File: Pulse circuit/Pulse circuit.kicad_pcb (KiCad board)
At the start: 4 copper layers, 76.9 x 88 mm, 9 parts, among them J1 Conn_01x02_Pin, U1 module_max30102, U2 module_max30102, U3 DOIT-ESP32-DEVKIT-V1

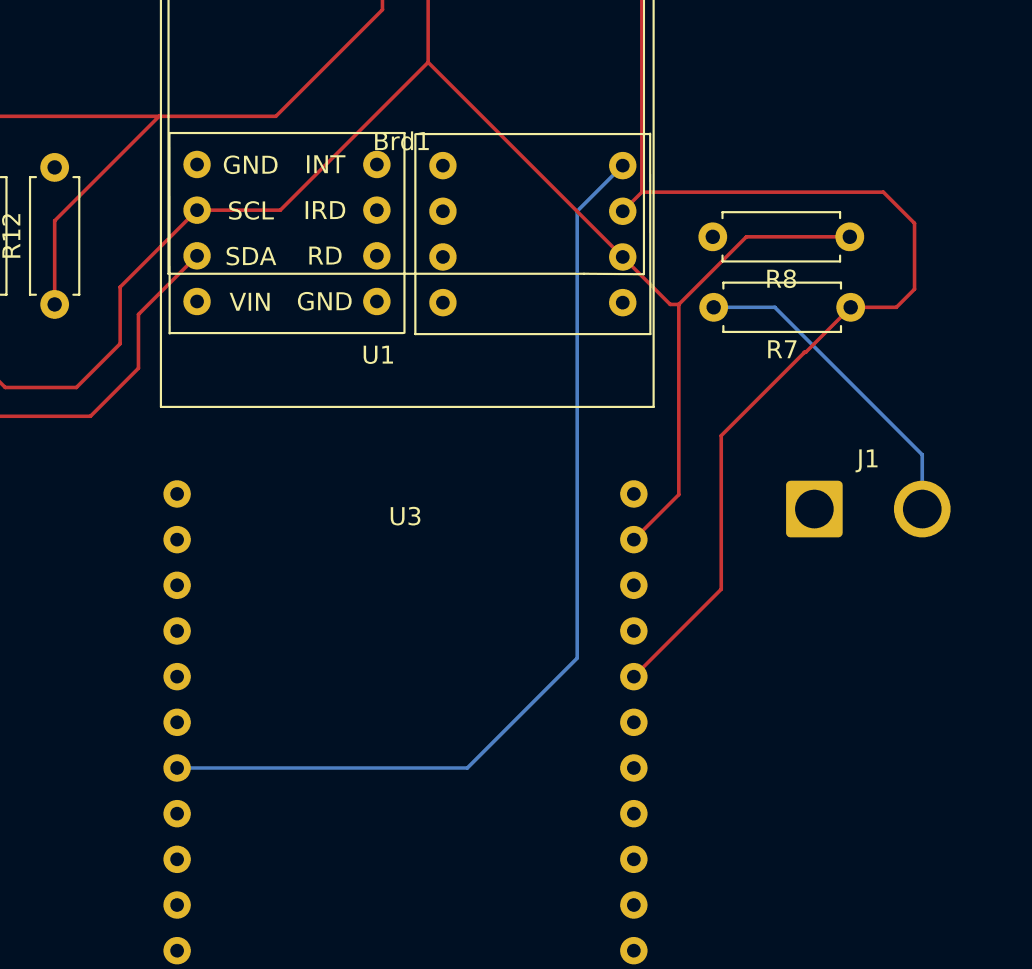
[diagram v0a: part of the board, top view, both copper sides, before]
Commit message: PCB new layer routed
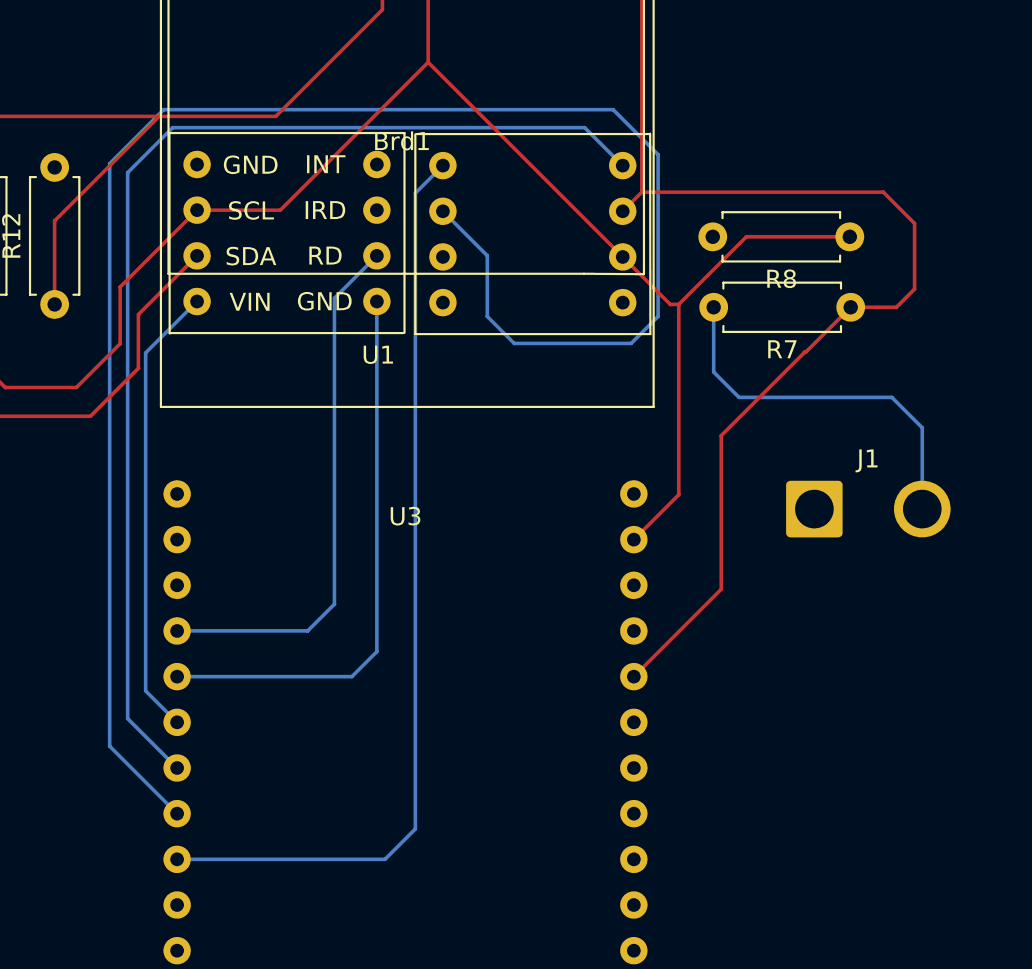
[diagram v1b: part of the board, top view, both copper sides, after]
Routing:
- net RD5v: track 0.00 -> 97.1 mm
- net IRD5v: track 0.02 -> 51.5 mm
- net IRD3v3: track 0.00 -> 31.2 mm
- net RD3v3: track 0.00 -> 29.7 mm
- net INT3v3: track 0.00 -> 25.3 mm
- net INT5v: track 53.2 -> 63.7 mm
- net 5V: track 91.2 -> 94.2 mm
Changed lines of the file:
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@@
 	)
 	(segment
-		(start 180.69 77.69)
-		(end 172.49 69.49)
-		(width 0.2)
-		(layer "B.Cu")
-		(net 5)
-	)
-	(segment
-		(start 180.69 80.71)
-		(end 180.69 77.69)
-		(width 0.2)
-		(layer "B.Cu")
-		(net 5)
-	)
-	(segment
-		(start 172.49 69.49)
-		(end 169.09 69.49)
+		(start 169.09 73.09)
+		(end 170.5 74.5)
+		(width 0.2)
+		(layer "B.Cu")
+		(net 5)
+	)
+	(segment
+		(start 180.69 76.19)
+		(end 180.69 80.71)
+		(width 0.2)
+		(layer "B.Cu")
+		(net 5)
+	)
+	(segment
+		(start 179 74.5)
+		(end 180.69 76.19)
+		(width 0.2)
+		(layer "B.Cu")
+		(net 5)
+	)
+	(segment
+		(start 170.5 74.5)
+		(end 179 74.5)
+		(width 0.2)
+		(layer "B.Cu")
+		(net 5)
+	)
+	(segment
+		(start 169.09 69.49)
+		(end 169.09 73.09)
 		(width 0.2)
 		(layer "B.Cu")
@@
 	)
 	(segment
-		(start 161.5 64.1425)
-		(end 161.5 89)
-		(width 0.2)
-		(layer "B.Cu")
-		(net 10)
-	)
-	(segment
-		(start 155.39 95.11)
-		(end 139.25 95.11)
-		(width 0.2)
-		(layer "B.Cu")
-		(net 10)
-	)
-	(segment
-		(start 161.5 89)
-		(end 155.39 95.11)
-		(width 0.2)
-		(layer "B.Cu")
-		(net 10)
-	)
-	(segment
-		(start 164.0325 61.61)
-		(end 161.5 64.1425)
-		(width 0.2)
-		(layer "B.Cu")
-		(net 10)
-	)
-	(segment
-		(start 139.27 100.19)
-		(end 139.25 100.19)
-		(width 0.2)
-		(layer "B.Cu")
+		(start 137.5 90.82)
+		(end 137.5 72.026684)
+		(width 0.2)
+		(layer "B.Cu")
+		(net 6)
+	)
+	(segment
+		(start 139.25 92.57)
+		(end 137.5 90.82)
+		(width 0.2)
+		(layer "B.Cu")
+		(net 6)
+	)
+	(segment
+		(start 137.5 72.026684)
+		(end 140.359184 69.1675)
+		(width 0.2)
+		(layer "B.Cu")
+		(net 6)
+	)
+	(segment
+		(start 150.359184 66.6275)
+		(end 148 68.986684)
+		(width 0.2)
+		(layer "B.Cu")
+		(net 7)
+	)
+	(segment
+		(start 146.49 87.49)
+		(end 139.25 87.49)
+		(width 0.2)
+		(layer "B.Cu")
+		(net 7)
+	)
+	(segment
+		(start 148 68.986684)
+		(end 148 86)
+		(width 0.2)
+		(layer "B.Cu")
+		(net 7)
+	)
+	(segment
+		(start 148 86)
+		(end 146.5 87.5)
+		(width 0.2)
+		(layer "B.Cu")
+		(net 7)
+	)
+	(segment
+		(start 146.5 87.5)
+		(end 146.49 87.49)
+		(width 0.2)
+		(layer "B.Cu")
+		(net 7)
+	)
+	(segment
+		(start 139.25 90.03)
+		(end 148.97 90.03)
+		(width 0.2)
+		(layer "B.Cu")
+		(net 8)
+	)
+	(segment
+		(start 148.97 90.03)
+		(end 150.359184 88.640816)
+		(width 0.2)
+		(layer "B.Cu")
+		(net 8)
+	)
+	(segment
+		(start 150.359184 88.640816)
+		(end 150.359184 69.1675)
+		(width 0.2)
+		(layer "B.Cu")
+		(net 8)
+	)
+	(segment
+		(start 139.25 97.65)
+		(end 135.5 93.9)
+		(width 0.2)
+		(layer "B.Cu")
+		(net 9)
+	)
+	(segment
+		(start 158 71.5)
+		(end 156.5 70)
+		(width 0.2)
+		(layer "B.Cu")
+		(net 9)
+	)
+	(segment
+		(start 135.5 61.5)
+		(end 138.5 58.5)
+		(width 0.2)
+		(layer "B.Cu")
+		(net 9)
+	)
+	(segment
+		(start 163.5 58.5)
+		(end 166 61)
+		(width 0.2)
+		(layer "B.Cu")
+		(net 9)
+	)
+	(segment
+		(start 135.5 93.9)
+		(end 135.5 61.5)
+		(width 0.2)
+		(layer "B.Cu")
+		(net 9)
+	)
+	(segment
+		(start 164.5 71.5)
+		(end 158 71.5)
+		(width 0.2)
+		(layer "B.Cu")
+		(net 9)
+	)
+	(segment
+		(start 138.5 58.5)
+		(end 163.5 58.5)
+		(width 0.2)
+		(layer "B.Cu")
+		(net 9)
+	)
+	(segment
+		(start 166 61)
+		(end 166 70)
+		(width 0.2)
+		(layer "B.Cu")
+		(net 9)
+	)
+	(segment
+		(start 156.5 66.6175)
+		(end 154.0325 64.15)
+		(width 0.2)
+		(layer "B.Cu")
+		(net 9)
+	)
+	(segment
+		(start 156.5 70)
+		(end 156.5 66.6175)
+		(width 0.2)
+		(layer "B.Cu")
+		(net 9)
+	)
+	(segment
+		(start 166 70)
+		(end 164.5 71.5)
+		(width 0.2)
+		(layer "B.Cu")
+		(net 9)
+	)
+	(segment
+		(start 136.5 62)
+		(end 139 59.5)
+		(width 0.2)
+		(layer "B.Cu")
+		(net 10)
+	)
+	(segment
+		(start 136.5 92.36)
+		(end 136.5 62)
+		(width 0.2)
+		(layer "B.Cu")
+		(net 10)
+	)
+	(segment
+		(start 139.25 95.11)
+		(end 136.5 92.36)
+		(width 0.2)
+		(layer "B.Cu")
+		(net 10)
+	)
+	(segment
+		(start 139 59.5)
+		(end 161.9225 59.5)
+		(width 0.2)
+		(layer "B.Cu")
+		(net 10)
+	)
+	(segment
+		(start 161.9225 59.5)
+		(end 164.0325 61.61)
+		(width 0.2)
+		(layer "B.Cu")
+		(net 10)
+	)
+	(segment
+		(start 150.81 100.19)
+		(end 152.5 98.5)
+		(width 0.2)
+		(layer "B.Cu")
+		(net 11)
+	)
+	(segment
+		(start 152.5 63.1425)
+		(end 154.0325 61.61)
+		(width 0.2)
+		(layer "B.Cu")
+		(net 11)
+	)
+	(segment
+		(start 139.25 100.19)
+		(end 150.81 100.19)
+		(width 0.2)
+		(layer "B.Cu")
+		(net 11)
+	)
+	(segment
+		(start 152.5 98.5)
+		(end 152.5 63.1425)
+		(width 0.2)
+		(layer "B.Cu")

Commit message: Made some changes to the GND & Power planes
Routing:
- net 5V: track 94.2 -> 21.6 mm
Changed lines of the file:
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@@
-	)
-	(segment
-		(start 139.25 123.05)
-		(end 156.82 105.48)
-		(width 0.2)
-		(layer "In1.Cu")
-		(net 5)
-	)
-	(segment
-		(start 156.82 105.48)
-		(end 156.82 84.85)
-		(width 0.2)
-		(layer "In1.Cu")
-		(net 5)
-	)
-	(segment
-		(start 156.82 84.85)
-		(end 164.0325 77.6375)
-		(width 0.2)
-		(layer "In1.Cu")
-		(net 5)
 	)
 	(segment
@@
 		(start 168.83 69.23)
 		(end 169.09 69.49)
-		(width 0.2)
-		(layer "In1.Cu")
-		(net 5)
-	)
-	(segment
-		(start 169.04 69.32)
-		(end 169.04 65.57)
-		(width 0.2)
-		(layer "In1.Cu")
-		(net 5)
-	)
-	(segment
-		(start 164.0325 77.6375)
-		(end 164.0325 69.23)
-		(width 0.2)
-		(layer "In1.Cu")
-		(net 5)
-	)
-	(segment
-		(start 164.0325 69.23)
-		(end 168.83 69.23)
 		(width 0.2)
 		(layer "In1.Cu")
@@
 		(layer "In1.Cu")
 		(hatch edge 0.5)
-		(priority 1)
+		(priority 2)
 		(connect_pads
 			(clearance 0.5)
@@
 		(polygon
 			(pts
-				(xy 125.95 62.7) (xy 125.82 58.73) (xy 138.08 58.87) (xy 137.94 51.47) (xy 154.65 50.92) (xy 154.38 45.51)
-				(xy 178.9 45.65) (xy 180.88 125.23) (xy 159.21 125.3) (xy 159.06 121.19) (xy 180.15 121.59) (xy 177.31 58.04)
-				(xy 151.19 58.22) (xy 151.38 72.24) (xy 146.22 72.2) (xy 146.17 67.77) (xy 150.1 67.77) (xy 149.82 59.36)
-				(xy 136.9 59.82) (xy 136.86 63.98) (xy 125.99 62.7)
+				(xy 126.1 62.42) (xy 126.1 60.01) (xy 148.32 59.9) (xy 147.91 51.73) (xy 154.514358 51.423511) (xy 154.364374 47.51396)
+				(xy 158.45 47.3) (xy 158.5 52.19) (xy 149.09 52.86) (xy 148.83 62.78) (xy 136.23 62.68) (xy 136.7 76.92)
+				(xy 155.59 77.55) (xy 160.38 121.83) (xy 166.08 121.9) (xy 166.150204 124.48) (xy 158.087831 124.48)
+				(xy 151.5 79.02) (xy 134.84 78.25) (xy 134.3 63.9) (xy 125.9 62.43)
 			)
 		)
@@
 		(layer "In1.Cu")
 		(hatch edge 0.5)
-		(priority 2)
+		(priority 1)
 		(connect_pads
 			(clearance 0.5)
@@
 		(polygon
 			(pts
-				(xy 167.44 63.84) (xy 171.36 63.93) (xy 171.27 72.47) (xy 165.11 72.15) (xy 165.06 78.77) (xy 157.44 85.8)
-				(xy 158.26 124.66) (xy 137.3 125.07) (xy 137.44 121.32) (xy 156.39 120.82) (xy 155.75 84.89) (xy 162.69 78.18)
-				(xy 162.78 67.81) (xy 167.48 67.72) (xy 167.44 63.88)
+				(xy 162.51 70.37) (xy 162.41 67.85) (xy 167.25 67.69) (xy 167.45 62.45) (xy 171.41 62.7) (xy 171.25 74.55)
+				(xy 184.29 74.39) (xy 184.44 85.5) (xy 178.35 85.58) (xy 177.5 77.25) (xy 171.02 76.94) (xy 171.18 127.23)
+				(xy 136 127.31) (xy 136 121.6) (xy 144.26 121.6) (xy 144.18 125.61) (xy 167.01 125.38) (xy 167.4 75.17)
+				(xy 162.54 75.01) (xy 162.46 70.31)
 			)
 		)
@@
 		(polygon
 			(pts
-				(xy 115.95 41.93) (xy 192.38 41.93) (xy 192.38 129.77) (xy 115.79 129.77)
+				(xy 115.64 42.09) (xy 192.38 41.93) (xy 192.38 129.77) (xy 115.79 129.77)
 			)
 		)
